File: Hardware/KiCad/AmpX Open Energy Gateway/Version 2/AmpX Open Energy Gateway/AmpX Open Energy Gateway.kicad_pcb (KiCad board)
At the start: 2 copper layers, 2 parts, among them U1 ESP32-C3-DevKitM-1

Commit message: feat: complete pcb design
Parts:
- removed U1: ESP32-C3-DevKitM-1, PCM_Espressif:ESP32-C3-DevKitM-1
- added J1: POW, Connector_JST:JST_XH_B2B-XH-A_1x02_P2.50mm_Vertical, F.Cu at (157.0, 109.0)
- added J3: STATUS, Connector_JST:JST_XH_B5B-XH-A_1x05_P2.50mm_Vertical, F.Cu at (157.1, 99.2)
- added U3: ESP32-DEVKITC-32U, ESP32-DEVKITC-32U:MODULE_ESP32-DEVKITC-32U, F.Cu at (128.6, 99.0)
- U2: value ~ -> W5500; footprint AmpX-Footprint-Library.pretty:Simple LED Module -> Module_Ethernet_LAN_W5500_Lite.3dshapes:Module_Ethernet_LAN_W5500_Lite
- moved U2 60.0 mm to (181.2, 109.2), turned to 90 degrees
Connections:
- U2 pad 1: 3V3 -> /MISO
- U2 pad 10: (no net) -> /SCLK
- U2 pad 11: (no net) -> /CS
- U2 pad 12: (no net) -> unconnected-(U2-INT-Pad12)
- U2 pad 2: Net-(U2-GND) -> unconnected-(U2-RESET-Pad2)
- U2 pad 4: (no net) -> +3.3V
- U2 pad 5: (no net) -> +3.3V
- U2 pad 6: (no net) -> GND
- U2 pad 7: (no net) -> GND
- U2 pad 8: (no net) -> GND
- U2 pad 9: (no net) -> /MOSI
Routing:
- net +5V: track 0.00 -> 60.7 mm
- net /CS: track 0.00 -> 59.6 mm
- net /SCLK: track 0.00 -> 58.9 mm
- net /MOSI: track 0.00 -> 42.8 mm
- net /POWER: track 0.00 -> 41.5 mm
- net +3.3V: track 0.00 -> 38.8 mm
- net /METER: track 0.00 -> 37.9 mm
- net /MISO: track 0.00 -> 37.3 mm
- net /WIFI: track 0.00 -> 34.3 mm
- net /INTERNET: track 0.00 -> 30.7 mm
- net /SERVER: track 0.00 -> 27.2 mm
- net GND: track 0.00 -> 0.02 mm, vias 0 -> 8
- added copper zone on B.Cu, net GND
- added copper zone on F.Cu, net GND
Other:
- board outline added: 86.5 x 33 mm
- board text added: "AmpX Open Energy Gateway"
- board text added: "Ver 1.0"

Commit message: created gerbers
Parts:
- added J3: Status Conn Top, Connector_Wire:SolderWire-0.5sqmm_1x06_P4.6mm_D0.9mm_OD2.1mm, F.Cu at (226.2, 106.1)
- added LED1: CMD15-21VGD/TR8, AmpX-Footprint-Library.pretty:LED_GREEN_CMD15-21_VCC, F.Cu at (223.8, 90.7)
- added LED2: CMD15-21VGD/TR8, AmpX-Footprint-Library.pretty:LED_GREEN_CMD15-21_VCC, F.Cu at (218.8, 90.7)
- added LED3: CMD15-21VGD/TR8, AmpX-Footprint-Library.pretty:LED_GREEN_CMD15-21_VCC, F.Cu at (213.8, 90.7)
- added LED4: CMD15-21VGD/TR8, AmpX-Footprint-Library.pretty:LED_GREEN_CMD15-21_VCC, F.Cu at (208.6, 90.7)
- added LED5: CMD15-21VGD/TR8, AmpX-Footprint-Library.pretty:LED_GREEN_CMD15-21_VCC, F.Cu at (203.8, 90.7)
- added R1: Resistor SMD DigiKey ERJ-T06J221V, AmpX-Footprint-Library.pretty:Resistor_SMD_Digikey_RESC2012X70N, F.Cu at (223.3, 96.9)
- added R2: Resistor SMD DigiKey ERJ-T06J221V, AmpX-Footprint-Library.pretty:Resistor_SMD_Digikey_RESC2012X70N, F.Cu at (219.0, 96.9)
- added R3: Resistor SMD DigiKey ERJ-T06J221V, AmpX-Footprint-Library.pretty:Resistor_SMD_Digikey_RESC2012X70N, F.Cu at (213.8, 96.9)
- added R4: Resistor SMD DigiKey ERJ-T06J221V, AmpX-Footprint-Library.pretty:Resistor_SMD_Digikey_RESC2012X70N, F.Cu at (208.8, 96.9)
- added R5: Resistor SMD DigiKey ERJ-T06J221V, AmpX-Footprint-Library.pretty:Resistor_SMD_Digikey_RESC2012X70N, F.Cu at (203.4, 96.9)
- renumbered J3 to J2
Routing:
- net Net-(J3-Pin_6): track 0.00 -> 41.3 mm
- net Net-(J3-Pin_4): track 0.00 -> 10.6 mm
- net Net-(J3-Pin_5): track 0.00 -> 10.0 mm
- net Net-(J3-Pin_3): track 0.00 -> 9.53 mm
- net Net-(J3-Pin_1): track 0.00 -> 9.38 mm
- net Net-(J3-Pin_2): track 0.00 -> 9.26 mm
- net Net-(LED1-Pad2): track 0.00 -> 4.09 mm
- net Net-(LED4-Pad2): track 0.00 -> 4.07 mm
- net Net-(LED5-Pad2): track 0.00 -> 4.06 mm
- net Net-(LED2-Pad2): track 0.00 -> 3.88 mm
- net Net-(LED3-Pad2): track 0.00 -> 3.77 mm
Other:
- board size 86.5 x 33 mm -> 136.1 x 33 mm

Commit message: feat: separate front and bottom pcbs
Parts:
- removed J3: Status Conn Top, Connector_Wire:SolderWire-0.5sqmm_1x06_P4.6mm_D0.9mm_OD2.1mm
- removed LED1, LED2, LED3, LED4, LED5: CMD15-21VGD/TR8, AmpX-Footprint-Library.pretty:LED_GREEN_CMD15-21_VCC
- removed R1, R2, R3, R4, R5: Resistor SMD DigiKey ERJ-T06J221V, AmpX-Footprint-Library.pretty:Resistor_SMD_Digikey_RESC2012X70N
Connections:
- net +5V renamed /+5V
- net GND renamed /GND
- U3 pad 26: /DE -> unconnected-(U3-IO4-Pad26)
- U3 pad 27: /RX -> unconnected-(U3-IO16-Pad27)
- U3 pad 28: /TX -> unconnected-(U3-IO17-Pad28)
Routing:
- net Net-(J3-Pin_6): track 41.3 -> 0.00 mm
- net Net-(J3-Pin_4): track 10.6 -> 0.00 mm
- net Net-(J3-Pin_5): track 10.0 -> 0.00 mm
- net Net-(J3-Pin_3): track 9.53 -> 0.00 mm
- net Net-(J3-Pin_1): track 9.38 -> 0.00 mm
- net Net-(J3-Pin_2): track 9.26 -> 0.00 mm
- net Net-(LED1-Pad2): track 4.09 -> 0.00 mm
- net Net-(LED4-Pad2): track 4.07 -> 0.00 mm
- net Net-(LED5-Pad2): track 4.06 -> 0.00 mm
- net Net-(LED2-Pad2): track 3.88 -> 0.00 mm
- net Net-(LED3-Pad2): track 3.77 -> 0.00 mm
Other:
- board size 136.1 x 33 mm -> 86.5 x 33 mm

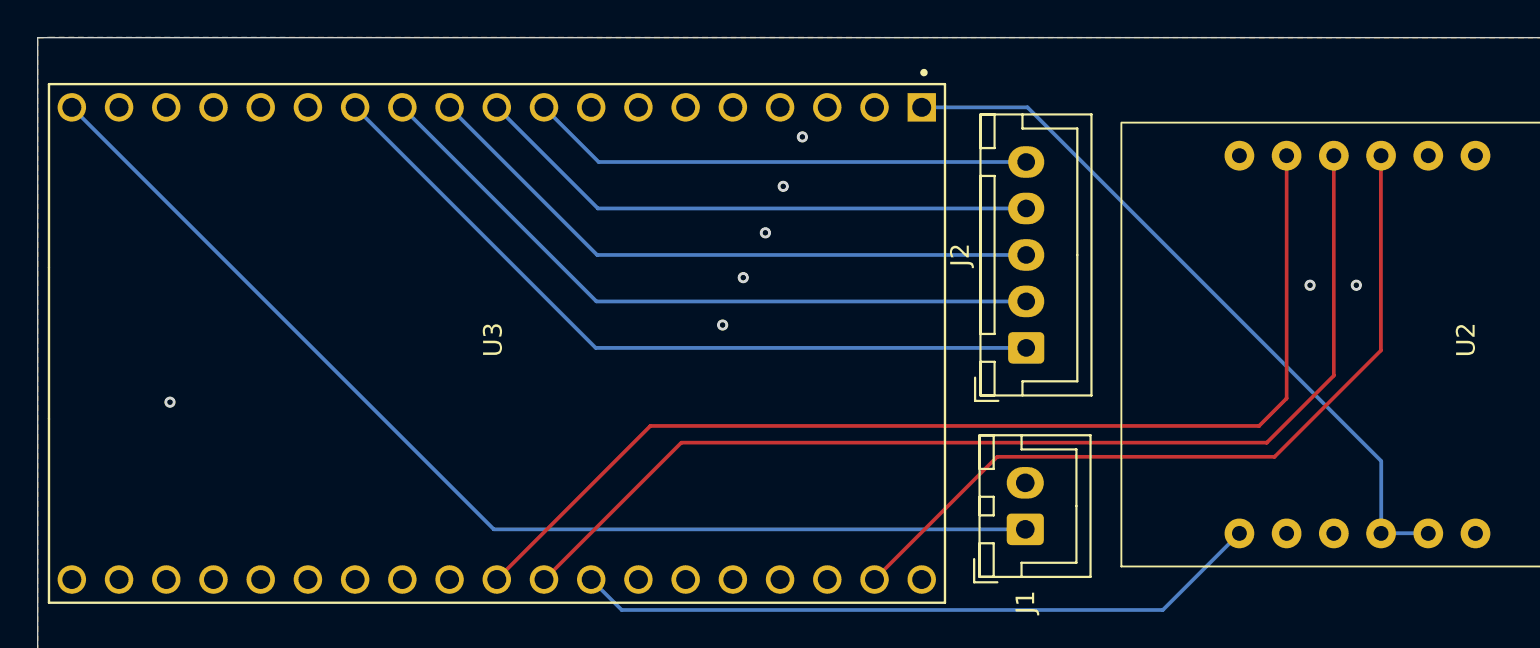
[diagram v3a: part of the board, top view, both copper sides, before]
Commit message: added extra wire for ground
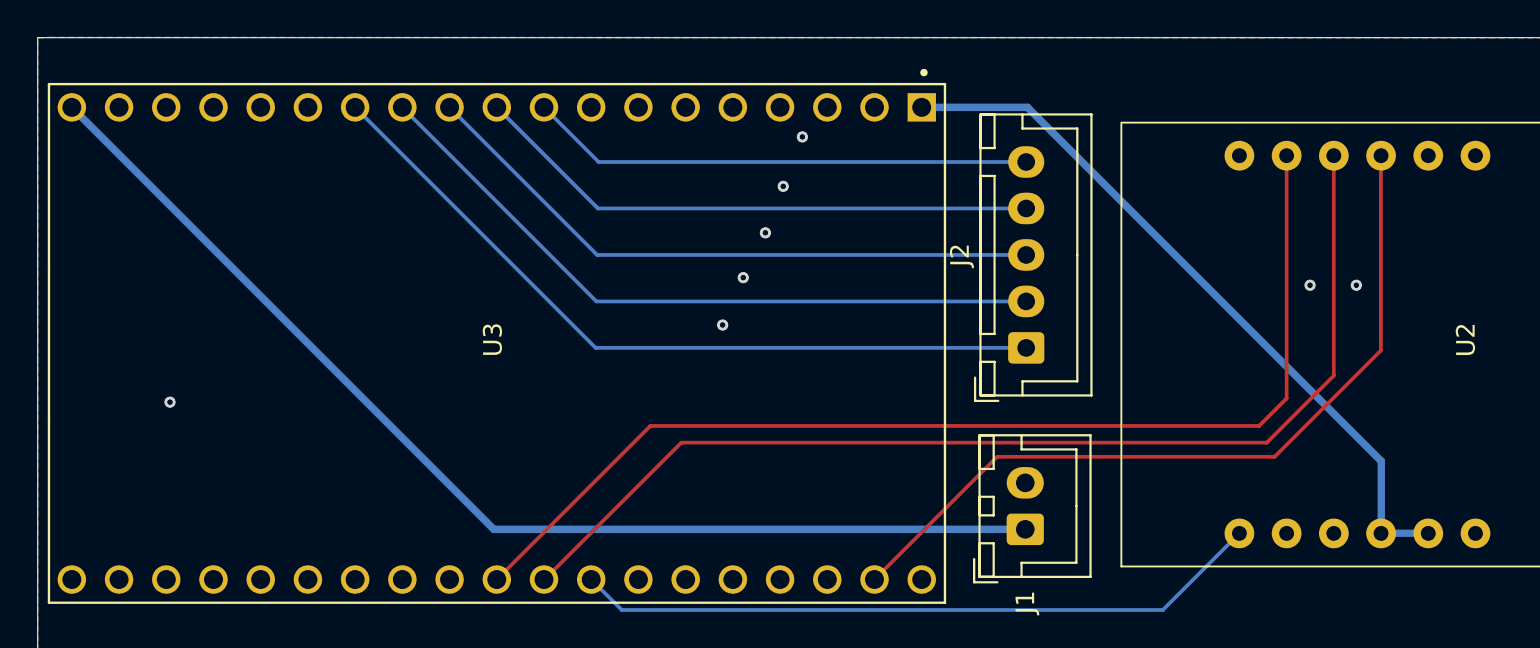
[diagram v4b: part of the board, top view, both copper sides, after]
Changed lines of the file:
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@@
 			(keep_text_aligned yes)
 		)
-		(gr_text "86.5"
+		(gr_text "86,5"
 			(at 147.13 120.85 0)
 			(layer "Dwgs.User")
@@
 		(start 151.44 86.26)
 		(end 157.13 86.26)
-		(width 0.2)
+		(width 0.4)
 		(layer "B.Cu")
 		(net 4)
@@
 		(start 176.16 109.17)
 		(end 178.5 109.17)
-		(width 0.2)
+		(width 0.4)
 		(layer "B.Cu")
 		(net 4)
@@
 		(start 176.16 105.29)
 		(end 176.16 109.17)
-		(width 0.2)
+		(width 0.4)
 		(layer "B.Cu")
 		(net 4)
@@
 		(start 157.13 86.26)
 		(end 176.16 105.29)
-		(width 0.2)
+		(width 0.4)
 		(layer "B.Cu")
 		(net 4)
@@
 		(start 128.42 108.96)
 		(end 157.01 108.96)
-		(width 0.2)
+		(width 0.4)
 		(layer "B.Cu")
 		(net 7)
@@
 		(start 105.72 86.26)
 		(end 128.42 108.96)
-		(width 0.2)
+		(width 0.4)
 		(layer "B.Cu")
 		(net 7)

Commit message: api update
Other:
- board text added: "AmpX Energy Gateway V 1.1"
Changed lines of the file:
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@@
 		(layer "Edge.Cuts")
+	)
+	(gr_text "AmpX Energy Gateway V 1.1"
+		(at 162.534 85.799 0)
+		(layer "F.Cu")
+		(effects
+			(font
+				(size 1.2 1.2)
+				(thickness 0.3)
+				(bold yes)
+			)
+			(justify left bottom)
+		)
 	)
 	(gr_text "AmpX Open Energy Gateway"
